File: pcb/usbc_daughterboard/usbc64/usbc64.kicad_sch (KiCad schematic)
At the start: 11 parts, among them J1 USB_C_Receptacle_USB2.0, J2 Conn_01x04, U1 ESDALD05UG4

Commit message: disconnect MP pads
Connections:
- net GND: no longer J2.MP
- no-connect marks 2 -> 3
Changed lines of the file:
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@@
   (no_connect (at 64.135 73.025))
   (no_connect (at 64.135 70.485))
+  (no_connect (at 159.385 53.975))
   (wire (pts (xy 109.22 62.865) (xy 110.49 62.865))
     (stroke (width 0) (type default) (color 0 0 0 0))
@@
   )
   (wire (pts (xy 106.68 62.865) (xy 109.22 62.865))
-    (stroke (width 0) (type default) (color 0 0 0 0))
-  )
-  (wire (pts (xy 159.385 53.975) (xy 159.385 55.245))
     (stroke (width 0) (type default) (color 0 0 0 0))
   )
@@
   (symbol (lib_id "power:GNDPWR") (at 122.555 71.755 0) (unit 1)
     (in_bom yes) (on_board yes)
-    (property "Reference" "#PWR?" (id 0) (at 122.555 76.835 0)
+    (property "Reference" "#PWR0111" (id 0) (at 122.555 76.835 0)
       (effects (font (size 1.27 1.27)) hide)
     )
@@
     (pin "8")
     (pin "9")
-  )
-  (symbol (lib_id "power:GND") (at 159.385 55.245 0) (unit 1)
-    (in_bom yes) (on_board yes)
-    (property "Reference" "#PWR0103" (id 0) (at 159.385 61.595 0)
-      (effects (font (size 1.27 1.27)) hide)
-    )
-    (property "Value" "GND" (id 1) (at 159.385 59.055 0))
-    (property "Footprint" "" (id 2) (at 159.385 55.245 0)
-      (effects (font (size 1.27 1.27)) hide)
-    )
-    (property "Datasheet" "" (id 3) (at 159.385 55.245 0)
-      (effects (font (size 1.27 1.27)) hide)
-    )
-    (pin "1")
   )
   (symbol (lib_id "Device:R_Small") (at 67.945 50.165 270) (unit 1)
@@
       (reference "#PWR0102") (unit 1) (value "GND") (footprint "")
     )
-    (path "/accaf20d-fb48-4bd4-a872-2657970dcb88"
-      (reference "#PWR0103") (unit 1) (value "GND") (footprint "")
-    )
     (path "/dd395997-e60e-49d7-89eb-a27b2fa000eb"
       (reference "#PWR0104") (unit 1) (value "+5V") (footprint "")
@@
       (reference "#PWR0110") (unit 1) (value "+5V") (footprint "")
     )
+    (path "/1d8f7fdb-8389-43b1-b989-77c6a75c91ea"
+      (reference "#PWR0111") (unit 1) (value "GNDPWR") (footprint "")
+    )
     (path "/0f5deb86-fcab-492d-905f-d8e47136ee96"
       (reference "#PWR0112") (unit 1) (value "GNDPWR") (footprint "")
@@
       (reference "#PWR0114") (unit 1) (value "GNDPWR") (footprint "")
     )
-    (path "/1d8f7fdb-8389-43b1-b989-77c6a75c91ea"
-      (reference "#PWR?") (unit 1) (value "GNDPWR") (footprint "")
-    )
     (path "/062791e6-12f0-44fc-90f6-45f64ecdec87"

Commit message: placeholder fuse footprint and Imax
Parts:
- F1: footprint (none) -> Fuse:Fuse_1206_3216Metric
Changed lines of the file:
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@@
     (property "Reference" "F1" (id 0) (at 85.725 40.64 90))
     (property "Value" "500mA" (id 1) (at 85.725 44.45 90))
-    (property "Footprint" "" (id 2) (at 90.805 41.275 0)
+    (property "Footprint" "Fuse:Fuse_1206_3216Metric" (id 2) (at 90.805 41.275 0)
       (effects (font (size 1.27 1.27)) (justify left) hide)
     )
@@
     )
     (path "/062791e6-12f0-44fc-90f6-45f64ecdec87"
-      (reference "F1") (unit 1) (value "500mA") (footprint "")
+      (reference "F1") (unit 1) (value "500mA") (footprint "Fuse:Fuse_1206_3216Metric")
     )
     (path "/22294464-5c73-43d3-ae56-8a26bed6f964"

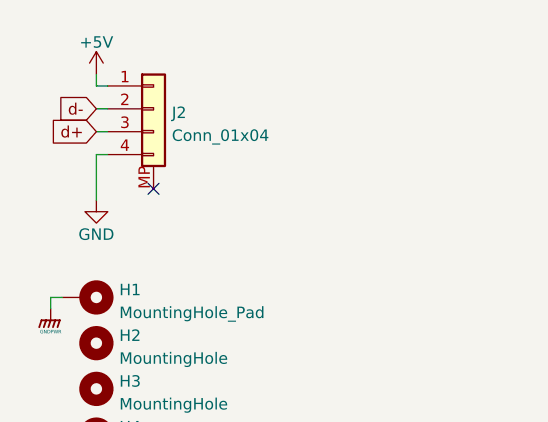
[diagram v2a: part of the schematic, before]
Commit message: add SH connector
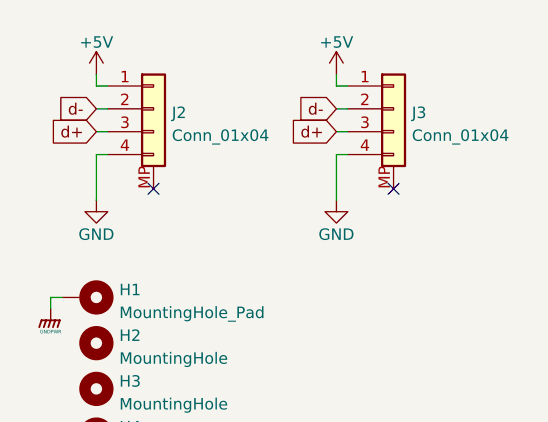
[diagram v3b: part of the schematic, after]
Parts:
- added J3: Conn_01x04, Connector_JST:JST_SH_SM04B-SRSS-TB_1x04-1MP_P1.00mm_Horizontal, symbol Connector_Generic:Conn_01x04
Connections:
- net +5V: now also J3.1 (Pin_1)
- net GND: now also J3.4 (Pin_4)
- net d+: now also J3.3 (Pin_3)
- net d-: now also J3.2 (Pin_2)
- no-connect marks 3 -> 4
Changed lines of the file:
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@@
   (junction (at 109.22 57.785) (diameter 0) (color 0 0 0 0)
   )
+  (no_connect (at 186.055 53.975))
   (no_connect (at 64.135 73.025))
   (no_connect (at 64.135 70.485))
@@
     (stroke (width 0) (type default) (color 0 0 0 0))
   )
+  (wire (pts (xy 179.705 47.625) (xy 180.975 47.625))
+    (stroke (width 0) (type default) (color 0 0 0 0))
+  )
   (wire (pts (xy 83.185 81.915) (xy 83.185 80.645))
     (stroke (width 0) (type default) (color 0 0 0 0))
@@
     (stroke (width 0) (type default) (color 0 0 0 0))
   )
+  (wire (pts (xy 179.705 41.275) (xy 179.705 42.545))
+    (stroke (width 0) (type default) (color 0 0 0 0))
+  )
   (wire (pts (xy 153.035 41.275) (xy 153.035 42.545))
     (stroke (width 0) (type default) (color 0 0 0 0))
@@
     (stroke (width 0) (type default) (color 0 0 0 0))
   )
+  (wire (pts (xy 180.975 50.165) (xy 179.705 50.165))
+    (stroke (width 0) (type default) (color 0 0 0 0))
+  )
   (wire (pts (xy 107.95 55.245) (xy 110.49 55.245))
     (stroke (width 0) (type default) (color 0 0 0 0))
@@
     (stroke (width 0) (type default) (color 0 0 0 0))
   )
+  (wire (pts (xy 179.705 45.085) (xy 180.975 45.085))
+    (stroke (width 0) (type default) (color 0 0 0 0))
+  )
   (wire (pts (xy 106.68 62.865) (xy 109.22 62.865))
     (stroke (width 0) (type default) (color 0 0 0 0))
@@
     (stroke (width 0) (type default) (color 0 0 0 0))
   )
+  (wire (pts (xy 179.705 42.545) (xy 180.975 42.545))
+    (stroke (width 0) (type default) (color 0 0 0 0))
+  )
+  (wire (pts (xy 179.705 50.165) (xy 179.705 55.245))
+    (stroke (width 0) (type default) (color 0 0 0 0))
+  )
   (wire (pts (xy 153.035 42.545) (xy 154.305 42.545))
     (stroke (width 0) (type default) (color 0 0 0 0))
@@
     )
   )
+  (global_label "d-" (shape input) (at 179.705 45.085 180) (fields_autoplaced)
+    (effects (font (size 1.27 1.27)) (justify right))
+    (property "Intersheet References" "${INTERSHEET_REFS}" (id 0) (at 174.5705 45.1644 0)
+      (effects (font (size 1.27 1.27)) (justify right) hide)
+    )
+  )
   (global_label "da+" (shape input) (at 133.35 57.785 0) (fields_autoplaced)
     (effects (font (size 1.27 1.27)) (justify left))
@@
     (effects (font (size 1.27 1.27)) (justify right))
     (property "Intersheet References" "${INTERSHEET_REFS}" (id 0) (at 109.2994 71.8095 90)
+      (effects (font (size 1.27 1.27)) (justify right) hide)
+    )
+  )
+  (global_label "d+" (shape input) (at 179.705 47.625 180) (fields_autoplaced)
+    (effects (font (size 1.27 1.27)) (justify right))
+    (property "Intersheet References" "${INTERSHEET_REFS}" (id 0) (at 174.5705 47.7044 0)
       (effects (font (size 1.27 1.27)) (justify right) hide)
     )
@@
     (pin "1")
   )
+  (symbol (lib_id "power:+5V") (at 179.705 41.275 0) (unit 1)
+    (in_bom yes) (on_board yes) (fields_autoplaced)
+    (property "Reference" "#PWR?" (id 0) (at 179.705 45.085 0)
+      (effects (font (size 1.27 1.27)) hide)
+    )
+    (property "Value" "+5V" (id 1) (at 179.705 37.6992 0))
+    (property "Footprint" "" (id 2) (at 179.705 41.275 0)
+      (effects (font (size 1.27 1.27)) hide)
+    )
+    (property "Datasheet" "" (id 3) (at 179.705 41.275 0)
+      (effects (font (size 1.27 1.27)) hide)
+    )
+    (pin "1")
+  )
   (symbol (lib_id "Mechanical:MountingHole") (at 153.035 81.28 0) (unit 1)
     (in_bom yes) (on_board yes) (fields_autoplaced)
@@
     )
     (pin "1")
+  )
+  (symbol (lib_id "Connector_Generic:Conn_01x04") (at 186.055 45.085 0) (unit 1)
+    (in_bom yes) (on_board yes) (fields_autoplaced)
+    (property "Reference" "J3" (id 0) (at 188.087 45.5203 0)
+      (effects (font (size 1.27 1.27)) (justify left))
+    )
+    (property "Value" "Conn_01x04" (id 1) (at 188.087 48.0572 0)
+      (effects (font (size 1.27 1.27)) (justify left))
+    )
+    (property "Footprint" "Connector_JST:JST_SH_SM04B-SRSS-TB_1x04-1MP_P1.00mm_Horizontal" (id 2) (at 186.055 45.085 0)
+      (effects (font (size 1.27 1.27)) hide)
+    )
+    (property "Datasheet" "~" (id 3) (at 186.055 45.085 0)
+      (effects (font (size 1.27 1.27)) hide)
+    )
+    (pin "1")
+    (pin "2")
+    (pin "3")
+    (pin "4")
+    (pin "MP")
   )
   (symbol (lib_id "Mechanical:MountingHole_Pad") (at 151.765 66.04 270) (unit 1)
@@
     )
     (property "Datasheet" "" (id 3) (at 73.66 51.435 0)
+      (effects (font (size 1.27 1.27)) hide)
+    )
+    (pin "1")
+  )
+  (symbol (lib_id "power:GND") (at 179.705 55.245 0) (unit 1)
+    (in_bom yes) (on_board yes)
+    (property "Reference" "#PWR?" (id 0) (at 179.705 61.595 0)
+      (effects (font (size 1.27 1.27)) hide)
+    )
+    (property "Value" "GND" (id 1) (at 179.705 59.055 0))
+    (property "Footprint" "" (id 2) (at 179.705 55.245 0)
+      (effects (font (size 1.27 1.27)) hide)
+    )
+    (property "Datasheet" "" (id 3) (at 179.705 55.245 0)
       (effects (font (size 1.27 1.27)) hide)
     )
@@
       (reference "#PWR0114") (unit 1) (value "GNDPWR") (footprint "")
     )
+    (path "/16fcd392-d1f5-436f-ac8a-30839f49d2b7"
+      (reference "#PWR?") (unit 1) (value "+5V") (footprint "")
+    )
+    (path "/48b2f0d9-af73-492f-bc34-bb84d4f5653c"
+      (reference "#PWR?") (unit 1) (value "GND") (footprint "")
+    )
     (path "/062791e6-12f0-44fc-90f6-45f64ecdec87"
       (reference "F1") (unit 1) (value "500mA") (footprint "Fuse:Fuse_1206_3216Metric")
@@
       (reference "J2") (unit 1) (value "Conn_01x04") (footprint "Connector_JST:JST_SUR_SM04B-SURS-TF_1x04-1MP_P0.80mm_Horizontal")
     )
+    (path "/1de4ded6-4f8b-4fe8-94b5-bce125dc0a0c"
+      (reference "J3") (unit 1) (value "Conn_01x04") (footprint "Connector_JST:JST_SH_SM04B-SRSS-TB_1x04-1MP_P1.00mm_Horizontal")
+    )
     (path "/2c0615eb-8c90-4863-b69f-db2bf5c67233"

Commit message: MP pads to GNDPWR
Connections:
- net GNDPWR: now also J2.MP, J3.MP
- no-connect marks 4 -> 2
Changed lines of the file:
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@@
   (junction (at 109.22 57.785) (diameter 0) (color 0 0 0 0)
   )
-  (no_connect (at 186.055 53.975))
   (no_connect (at 64.135 73.025))
   (no_connect (at 64.135 70.485))
-  (no_connect (at 159.385 53.975))
   (wire (pts (xy 109.22 62.865) (xy 110.49 62.865))
     (stroke (width 0) (type default) (color 0 0 0 0))
@@
     (stroke (width 0) (type default) (color 0 0 0 0))
   )
+  (wire (pts (xy 159.385 53.975) (xy 159.385 55.245))
+    (stroke (width 0) (type default) (color 0 0 0 0))
+  )
   (wire (pts (xy 73.66 50.165) (xy 73.66 47.625))
     (stroke (width 0) (type default) (color 0 0 0 0))
@@
   )
   (wire (pts (xy 179.705 42.545) (xy 180.975 42.545))
+    (stroke (width 0) (type default) (color 0 0 0 0))
+  )
+  (wire (pts (xy 186.055 53.975) (xy 186.055 55.245))
     (stroke (width 0) (type default) (color 0 0 0 0))
   )
@@
   (symbol (lib_id "power:+5V") (at 179.705 41.275 0) (unit 1)
     (in_bom yes) (on_board yes) (fields_autoplaced)
-    (property "Reference" "#PWR?" (id 0) (at 179.705 45.085 0)
+    (property "Reference" "#PWR0115" (id 0) (at 179.705 45.085 0)
       (effects (font (size 1.27 1.27)) hide)
     )
@@
   (symbol (lib_id "power:GND") (at 179.705 55.245 0) (unit 1)
     (in_bom yes) (on_board yes)
-    (property "Reference" "#PWR?" (id 0) (at 179.705 61.595 0)
+    (property "Reference" "#PWR0103" (id 0) (at 179.705 61.595 0)
       (effects (font (size 1.27 1.27)) hide)
     )
@@
     (pin "2")
   )
+  (symbol (lib_id "power:GNDPWR") (at 159.385 55.245 0) (unit 1)
+    (in_bom yes) (on_board yes)
+    (property "Reference" "#PWR?" (id 0) (at 159.385 60.325 0)
+      (effects (font (size 1.27 1.27)) hide)
+    )
+    (property "Value" "GNDPWR" (id 1) (at 159.385 57.785 0)
+      (effects (font (size 0.381 0.381)))
+    )
+    (property "Footprint" "" (id 2) (at 159.385 56.515 0)
+      (effects (font (size 1.27 1.27)) hide)
+    )
+    (property "Datasheet" "" (id 3) (at 159.385 56.515 0)
+      (effects (font (size 1.27 1.27)) hide)
+    )
+    (pin "1")
+  )
   (symbol (lib_id "power:+5V") (at 92.075 41.275 0) (unit 1)
     (in_bom yes) (on_board yes) (fields_autoplaced)
@@
     )
     (property "Datasheet" "" (id 3) (at 153.035 41.275 0)
+      (effects (font (size 1.27 1.27)) hide)
+    )
+    (pin "1")
+  )
+  (symbol (lib_id "power:GNDPWR") (at 186.055 55.245 0) (unit 1)
+    (in_bom yes) (on_board yes)
+    (property "Reference" "#PWR?" (id 0) (at 186.055 60.325 0)
+      (effects (font (size 1.27 1.27)) hide)
+    )
+    (property "Value" "GNDPWR" (id 1) (at 186.055 57.785 0)
+      (effects (font (size 0.381 0.381)))
+    )
+    (property "Footprint" "" (id 2) (at 186.055 56.515 0)
+      (effects (font (size 1.27 1.27)) hide)
+    )
+    (property "Datasheet" "" (id 3) (at 186.055 56.515 0)
       (effects (font (size 1.27 1.27)) hide)
     )
@@
       (reference "#PWR0102") (unit 1) (value "GND") (footprint "")
     )
+    (path "/48b2f0d9-af73-492f-bc34-bb84d4f5653c"
+      (reference "#PWR0103") (unit 1) (value "GND") (footprint "")
+    )
     (path "/dd395997-e60e-49d7-89eb-a27b2fa000eb"
       (reference "#PWR0104") (unit 1) (value "+5V") (footprint "")
@@
     )
     (path "/16fcd392-d1f5-436f-ac8a-30839f49d2b7"
-      (reference "#PWR?") (unit 1) (value "+5V") (footprint "")
-    )
-    (path "/48b2f0d9-af73-492f-bc34-bb84d4f5653c"
-      (reference "#PWR?") (unit 1) (value "GND") (footprint "")
+      (reference "#PWR0115") (unit 1) (value "+5V") (footprint "")
+    )
+    (path "/c1316690-7f6b-4786-9e0f-6a8acf97b1df"
+      (reference "#PWR?") (unit 1) (value "GNDPWR") (footprint "")
+    )
+    (path "/e7880dc5-89aa-4b41-be2d-83e1d26de574"
+      (reference "#PWR?") (unit 1) (value "GNDPWR") (footprint "")
     )
     (path "/062791e6-12f0-44fc-90f6-45f64ecdec87"
